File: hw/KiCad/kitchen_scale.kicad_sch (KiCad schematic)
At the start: 12 parts, among them J1 Conn_01x08_Socket, J2 Conn_HX711, J3 Conn_01x04_Pin, SW1 SW_Push, SW2 SW_SPST, SW3 SW_Push, SW4 SW_Push, U1 DEBO1_3_7LI_1_0A charge_contr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, U2 WeMos_D1_mini, U3 LF33_TO220

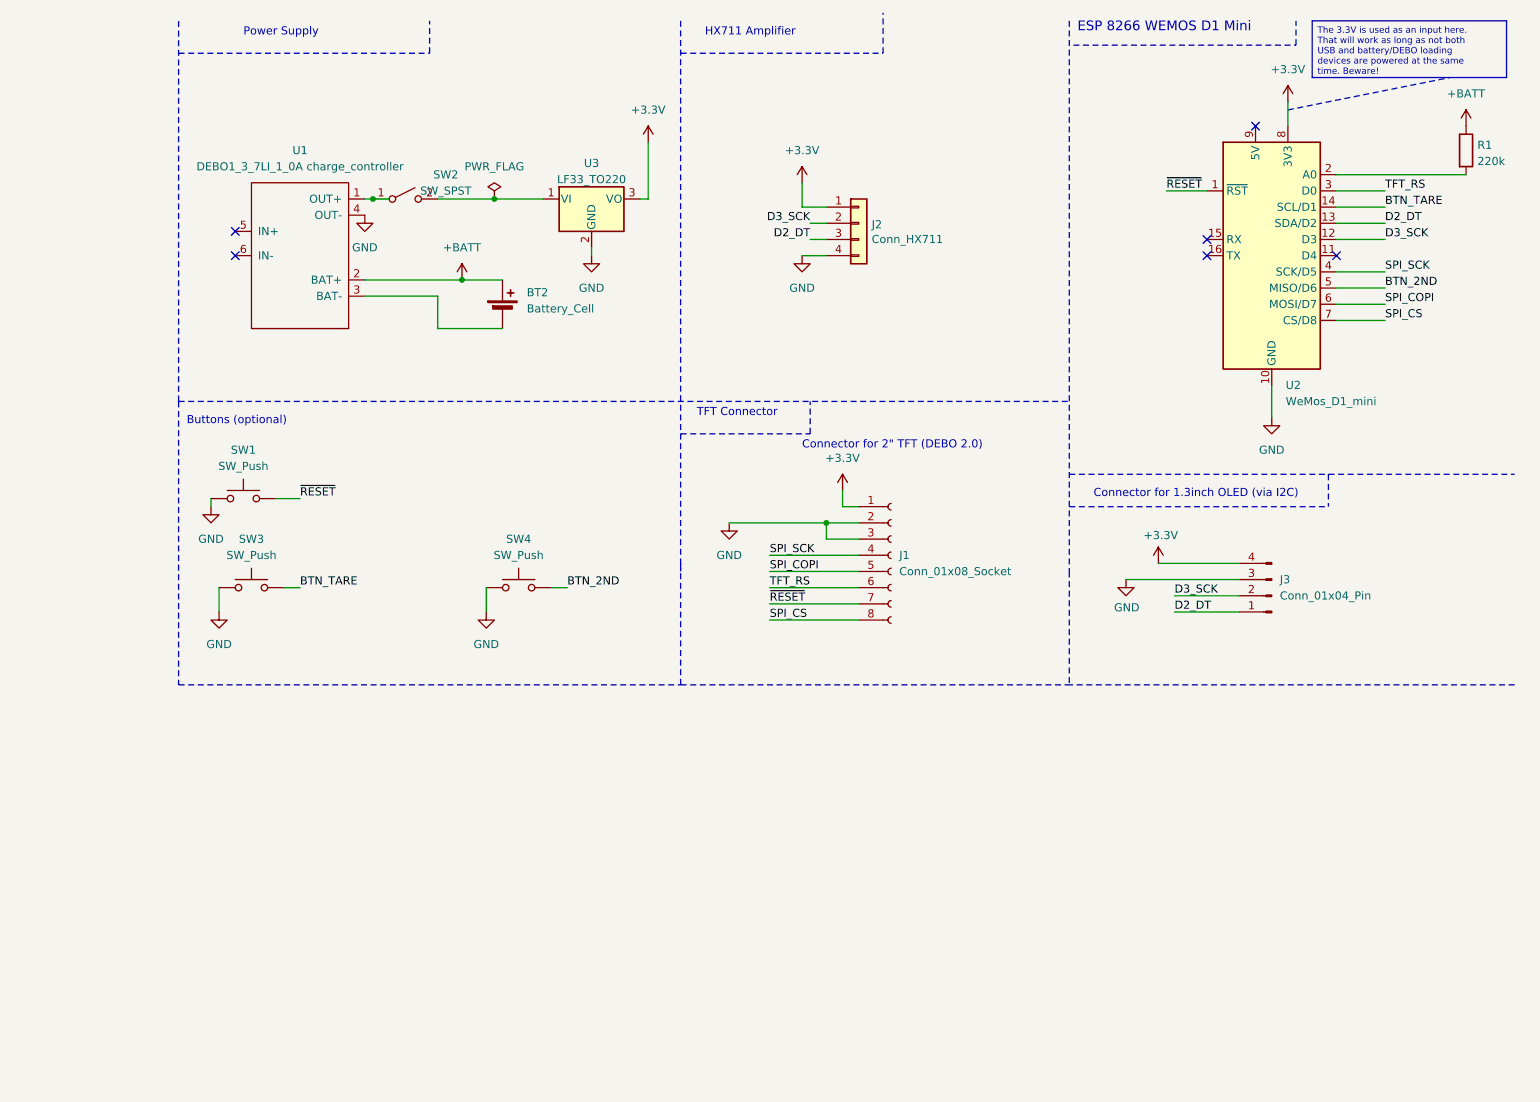
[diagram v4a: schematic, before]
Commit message: Add Hx711 module (not fully connected) for reference
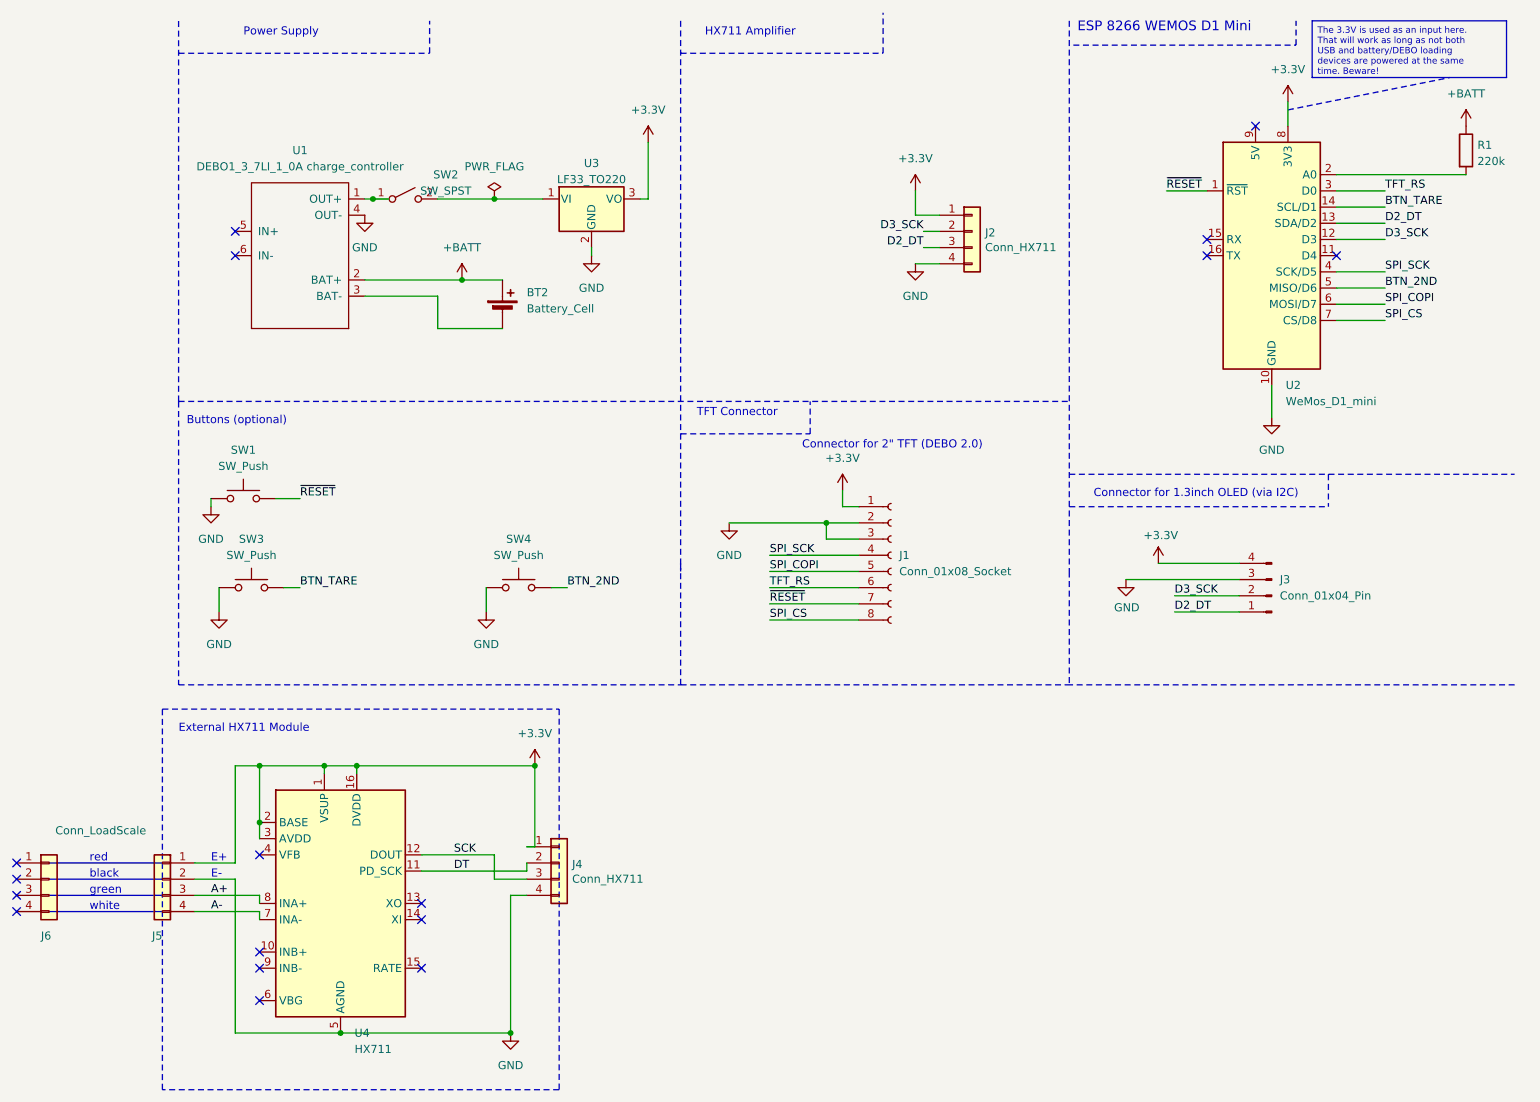
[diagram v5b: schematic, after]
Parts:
- added J4, J6: Conn_HX711, Connector_PinSocket_2.54mm:PinSocket_1x04_P2.54mm_Vertical, symbol Connector_Generic:Conn_01x04
- added J5: Conn_LoadScale, Connector_PinSocket_2.54mm:PinSocket_1x04_P2.54mm_Vertical, symbol Connector_Generic:Conn_01x04
- added U4: HX711, Package_SO:SOP-16_3.9x9.9mm_P1.27mm, symbol Analog_ADC:HX711
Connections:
- net +3.3V: now also J4.1 (Pin_1), J5.1 (Pin_1), U4.1 (VSUP), U4.16 (DVDD), U4.2 (BASE), U4.3 (AVDD)
- net GND: now also J4.4 (Pin_4), J5.2 (Pin_2), U4.5 (AGND)
- new net A+: J5.3 (Pin_3), U4.8 (INA+)
- new net A-: J5.4 (Pin_4), U4.7 (INA-)
- new net DT: J4.2 (Pin_2), U4.11 (PD_SCK)
- new net SCK: J4.3 (Pin_3), U4.12 (DOUT)
- no-connect marks 6 -> 17
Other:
- note added: "E+"
- note added: "E-"
- note added: "External HX711 Module"
- note added: "black"
- note added: "green"
- note added: "red"
- note added: "white"
- moved on the sheet: J2

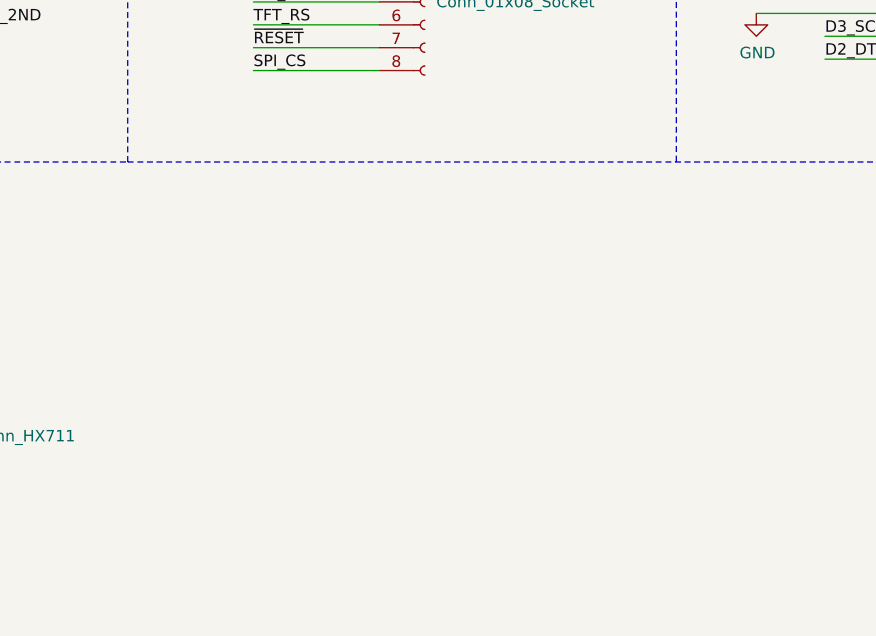
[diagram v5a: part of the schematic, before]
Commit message: Add: switch to 1.77" AzDelivery display with ST7789 processor. Seems working.
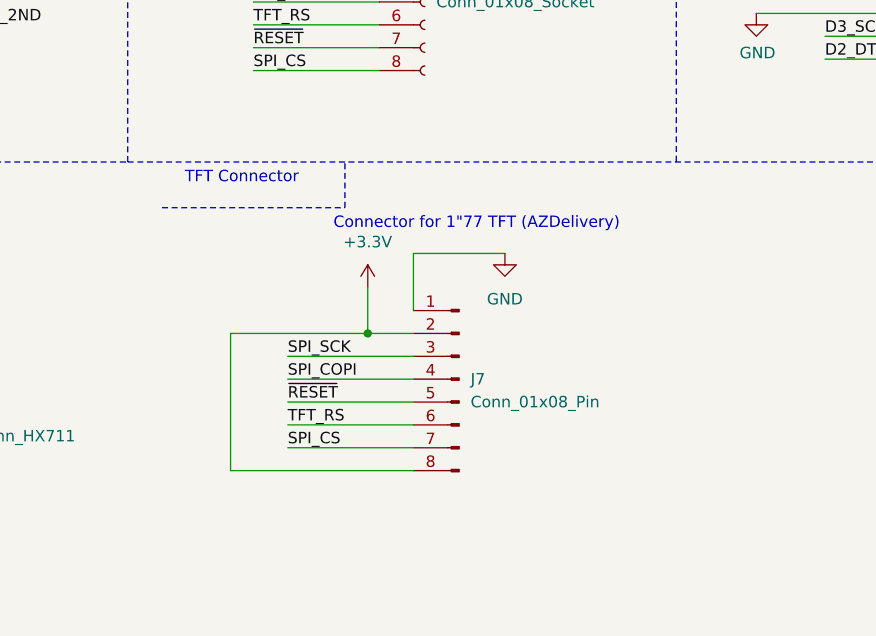
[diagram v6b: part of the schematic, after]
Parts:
- added J7: Conn_01x08_Pin, symbol Connector:Conn_01x08_Pin
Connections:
- net +3.3V: now also J7.2 (Pin_2), J7.8 (Pin_8)
- net GND: now also J7.1 (Pin_1)
- net SPI_COPI: now also J7.4 (Pin_4)
- net SPI_CS: now also J7.7 (Pin_7)
- net SPI_SCK: now also J7.3 (Pin_3)
- net TFT_RS: now also J7.6 (Pin_6)
- net ~{RESET}: now also J7.5 (Pin_5)
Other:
- note added: "Connector for 1"77 TFT (AZDelivery)"
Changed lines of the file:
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@@
   (junction (at 130.81 129.54) (diameter 0) (color 0 0 0 0)
+  )
+  (junction (at 180.34 135.89) (diameter 0) (color 0 0 0 0)
   )
   (junction (at 124.46 40.64) (diameter 0) (color 0 0 0 0)
@@
     (stroke (width 0) (type default))
   )
+  (wire (pts (xy 171.45 148.59) (xy 185.42 148.59))
+    (stroke (width 0) (type default))
+  )
   (wire (pts (xy 133.35 101.6) (xy 135.89 101.6))
     (stroke (width 0) (type default))
   )
+  (wire (pts (xy 195.58 127) (xy 185.42 127))
+    (stroke (width 0) (type default))
+  )
   (wire (pts (xy 176.53 91.44) (xy 176.53 93.98))
     (stroke (width 0) (type default))
@@
   (wire (pts (xy 256.54 46.99) (xy 264.16 46.99))
     (stroke (width 0) (type default))
+  )
+  (polyline (pts (xy 177.8 121.92) (xy 177.8 116.84))
+    (stroke (width 0) (type dash))
   )
   (polyline (pts (xy 72.39 120.65) (xy 134.62 120.65))
@@
     (stroke (width 0) (type default))
   )
+  (polyline (pts (xy 157.48 121.92) (xy 177.8 121.92))
+    (stroke (width 0) (type dash))
+  )
+  (wire (pts (xy 180.34 130.81) (xy 180.34 135.89))
+    (stroke (width 0) (type default))
+  )
   (wire (pts (xy 105.41 40.64) (xy 107.95 40.64))
     (stroke (width 0) (type default))
@@
     (stroke (width 0) (type dash))
   )
+  (wire (pts (xy 180.34 135.89) (xy 185.42 135.89))
+    (stroke (width 0) (type default))
+  )
   (wire (pts (xy 83.82 129.54) (xy 87.63 129.54))
     (stroke (width 0) (type default))
   )
+  (wire (pts (xy 171.45 138.43) (xy 185.42 138.43))
+    (stroke (width 0) (type default))
+  )
   (wire (pts (xy 87.63 138.43) (xy 87.63 140.97))
+    (stroke (width 0) (type default))
+  )
+  (wire (pts (xy 165.1 135.89) (xy 165.1 151.13))
     (stroke (width 0) (type default))
   )
@@
     (stroke (width 0) (type default))
   )
+  (wire (pts (xy 180.34 135.89) (xy 165.1 135.89))
+    (stroke (width 0) (type default))
+  )
+  (wire (pts (xy 171.45 143.51) (xy 185.42 143.51))
+    (stroke (width 0) (type default))
+  )
   (polyline (pts (xy 153.67 17.78) (xy 185.42 17.78))
     (stroke (width 0) (type dash))
@@
     (stroke (width 0) (type default))
   )
+  (wire (pts (xy 171.45 146.05) (xy 185.42 146.05))
+    (stroke (width 0) (type default))
+  )
   (wire (pts (xy 113.03 146.05) (xy 129.54 146.05))
     (stroke (width 0) (type default))
@@
     (stroke (width 0) (type default))
   )
+  (wire (pts (xy 171.45 140.97) (xy 185.42 140.97))
+    (stroke (width 0) (type default))
+  )
   (wire (pts (xy 248.92 25.4) (xy 248.92 29.21))
     (stroke (width 0) (type default))
@@
     (stroke (width 0) (type dash))
   )
+  (wire (pts (xy 185.42 127) (xy 185.42 133.35))
+    (stroke (width 0) (type default))
+  )
   (wire (pts (xy 77.47 152.4) (xy 87.63 152.4))
     (stroke (width 0) (type default))
@@
   (polyline (pts (xy 74.93 17.78) (xy 114.3 17.78))
     (stroke (width 0) (type dash))
+  )
+  (wire (pts (xy 165.1 151.13) (xy 185.42 151.13))
+    (stroke (width 0) (type default))
   )
   (wire (pts (xy 77.47 149.86) (xy 87.63 149.86))
@@
     (effects (font (size 1.27 1.27)) (justify left bottom))
   )
+  (text "TFT Connector" (at 160.02 119.38 0)
+    (effects (font (size 1.27 1.27)) (justify left bottom))
+  )
+  (text "Connector for 1\"77 TFT (AZDelivery)" (at 176.53 124.46 0)
+    (effects (font (size 1.27 1.27)) (justify left bottom))
+  )
   (label "BTN_2ND" (at 135.89 101.6 0) (fields_autoplaced)
     (effects (font (size 1.27 1.27)) (justify left bottom))
   )
   (label "SPI_SCK" (at 264.16 52.07 0) (fields_autoplaced)
+    (effects (font (size 1.27 1.27)) (justify left bottom))
+  )
+  (label "TFT_RS" (at 171.45 146.05 0) (fields_autoplaced)
     (effects (font (size 1.27 1.27)) (justify left bottom))
   )
@@
     (effects (font (size 1.27 1.27)) (justify right bottom))
   )
+  (label "SPI_SCK" (at 171.45 138.43 0) (fields_autoplaced)
+    (effects (font (size 1.27 1.27)) (justify left bottom))
+  )
   (label "SPI_SCK" (at 167.64 96.52 0) (fields_autoplaced)
     (effects (font (size 1.27 1.27)) (justify left bottom))
@@
     (effects (font (size 1.27 1.27)) (justify left bottom))
   )
+  (label "SPI_CS" (at 171.45 148.59 0) (fields_autoplaced)
+    (effects (font (size 1.27 1.27)) (justify left bottom))
+  )
   (label "SPI_CS" (at 167.64 106.68 0) (fields_autoplaced)
     (effects (font (size 1.27 1.27)) (justify left bottom))
@@
     (effects (font (size 1.27 1.27)) (justify left bottom))
   )
+  (label "SPI_COPI" (at 171.45 140.97 0) (fields_autoplaced)
+    (effects (font (size 1.27 1.27)) (justify left bottom))
+  )
   (label "SPI_CS" (at 264.16 59.69 0) (fields_autoplaced)
+    (effects (font (size 1.27 1.27)) (justify left bottom))
+  )
+  (label "~{RESET}" (at 171.45 143.51 0) (fields_autoplaced)
     (effects (font (size 1.27 1.27)) (justify left bottom))
   )
@@
     )
   )
+  (symbol (lib_id "power:+3.3V") (at 180.34 130.81 0) (unit 1)
+    (in_bom yes) (on_board yes) (dnp no) (fields_autoplaced)
+    (property "Reference" "#PWR020" (at 180.34 134.62 0)
+      (effects (font (size 1.27 1.27)) hide)
+    )
+    (property "Value" "+3.3V" (at 180.34 125.73 0)
+      (effects (font (size 1.27 1.27)))
+    )
+    (property "Footprint" "" (at 180.34 130.81 0)
+      (effects (font (size 1.27 1.27)) hide)
+    )
+    (property "Datasheet" "" (at 180.34 130.81 0)
+      (effects (font (size 1.27 1.27)) hide)
+    )
+    (pin "1")
+    (instances
+      (project "kitchen_scale"
+        (path "/cef6f603-8a0b-4dd0-af99-ebfbef7d1b4b"
+          (reference "#PWR020") (unit 1)
+        )
+      )
+    )
+  )
   (symbol (lib_id "power:+3.3V") (at 179.07 86.36 0) (unit 1)
     (in_bom yes) (on_board yes) (dnp no) (fields_autoplaced)
@@
         (path "/cef6f603-8a0b-4dd0-af99-ebfbef7d1b4b"
           (reference "SW1") (unit 1)
+        )
+      )
+    )
+  )
+  (symbol (lib_name "GND_2") (lib_id "power:GND") (at 195.58 127 0) (unit 1)
+    (in_bom yes) (on_board yes) (dnp no) (fields_autoplaced)
+    (property "Reference" "#PWR019" (at 195.58 133.35 0)
+      (effects (font (size 1.27 1.27)) hide)
+    )
+    (property "Value" "GND" (at 195.58 132.08 0)
+      (effects (font (size 1.27 1.27)))
+    )
+    (property "Footprint" "" (at 195.58 127 0)
+      (effects (font (size 1.27 1.27)) hide)
+    )
+    (property "Datasheet" "" (at 195.58 127 0)
+      (effects (font (size 1.27 1.27)) hide)
+    )
+    (pin "1")
+    (instances
+      (project "kitchen_scale"
+        (path "/cef6f603-8a0b-4dd0-af99-ebfbef7d1b4b"
+          (reference "#PWR019") (unit 1)
         )
       )
@@
         )
       )
+    )
+  )
+  (symbol (lib_id "Connector:Conn_01x08_Pin") (at 190.5 140.97 0) (mirror y) (unit 1)
+    (in_bom yes) (on_board yes) (dnp no) (fields_autoplaced)
+    (property "Reference" "J7" (at 191.77 140.97 0)
+      (effects (font (size 1.27 1.27)) (justify right))
+    )
+    (property "Value" "Conn_01x08_Pin" (at 191.77 143.51 0)
+      (effects (font (size 1.27 1.27)) (justify right))
+    )
+    (property "Footprint" "" (at 190.5 140.97 0)
+      (effects (font (size 1.27 1.27)) hide)
+    )
+    (property "Datasheet" "~" (at 190.5 140.97 0)
+      (effects (font (size 1.27 1.27)) hide)
+    )
+    (pin "8")
+    (pin "7")
+    (pin "2")
+    (pin "1")
+    (pin "5")
+    (pin "3")
+    (pin "4")
+    (pin "6")
+    (instances
+      (project "kitchen_scale"
+        (path "/cef6f603-8a0b-4dd0-af99-ebfbef7d1b4b"
+          (reference "J7") (unit 1)
+        )
+      )
